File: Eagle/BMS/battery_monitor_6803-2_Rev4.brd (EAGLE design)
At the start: 88.1 x 53.3 mm, 65 parts, among them Q1 MOSFET-PCHANNELIRLML2244, Q10 IRF9530, Q2 MOSFET-NCHANNELBSS138, Q3 MOSFET-PCHANNELIRLML2244, Q4 MOSFET-PCHANNELIRLML2244, Q5 MOSFET-PCHANNELIRLML2244, Q6 MOSFET-NCHANNELBSS138, Q7 MOSFET-NCHANNELBSS138, Q8 MOSFET-NCHANNELBSS138, Q9 PMOS_AO4435

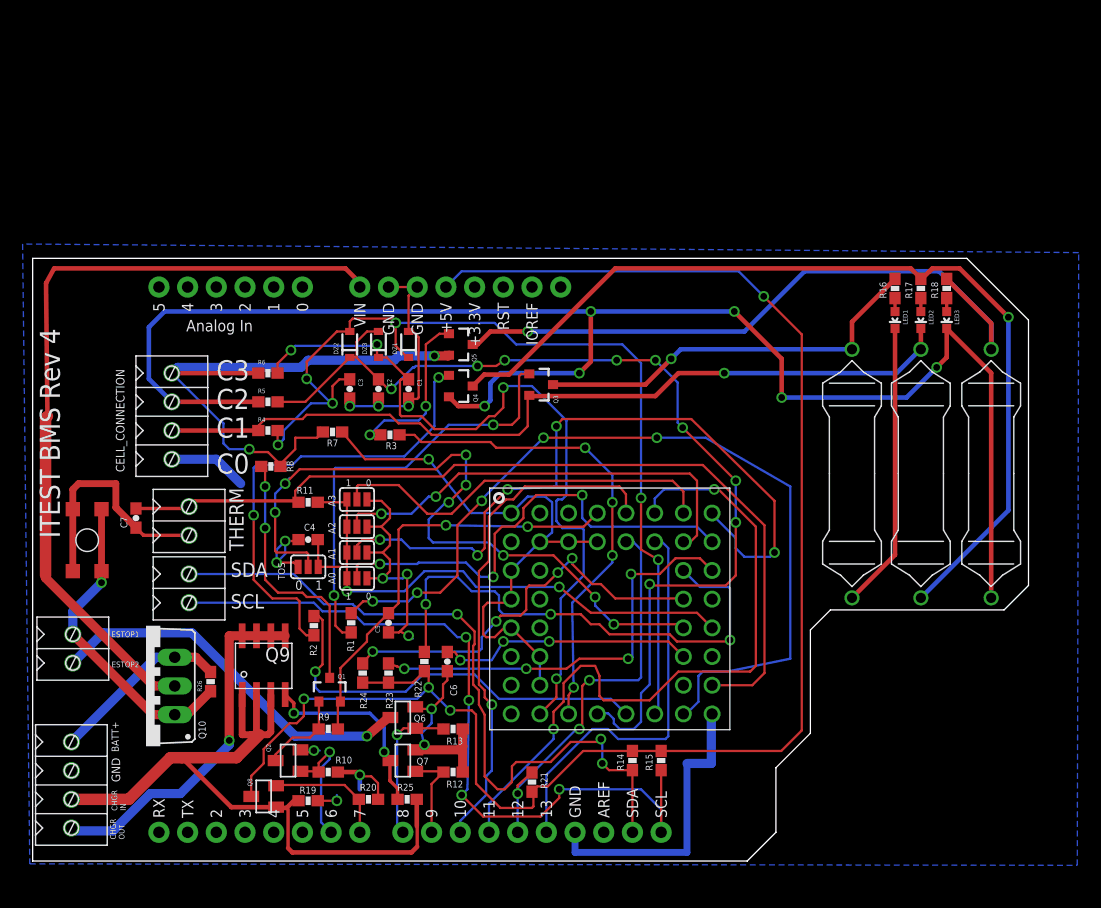
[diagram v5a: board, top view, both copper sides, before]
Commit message: Created encoder board for Layla
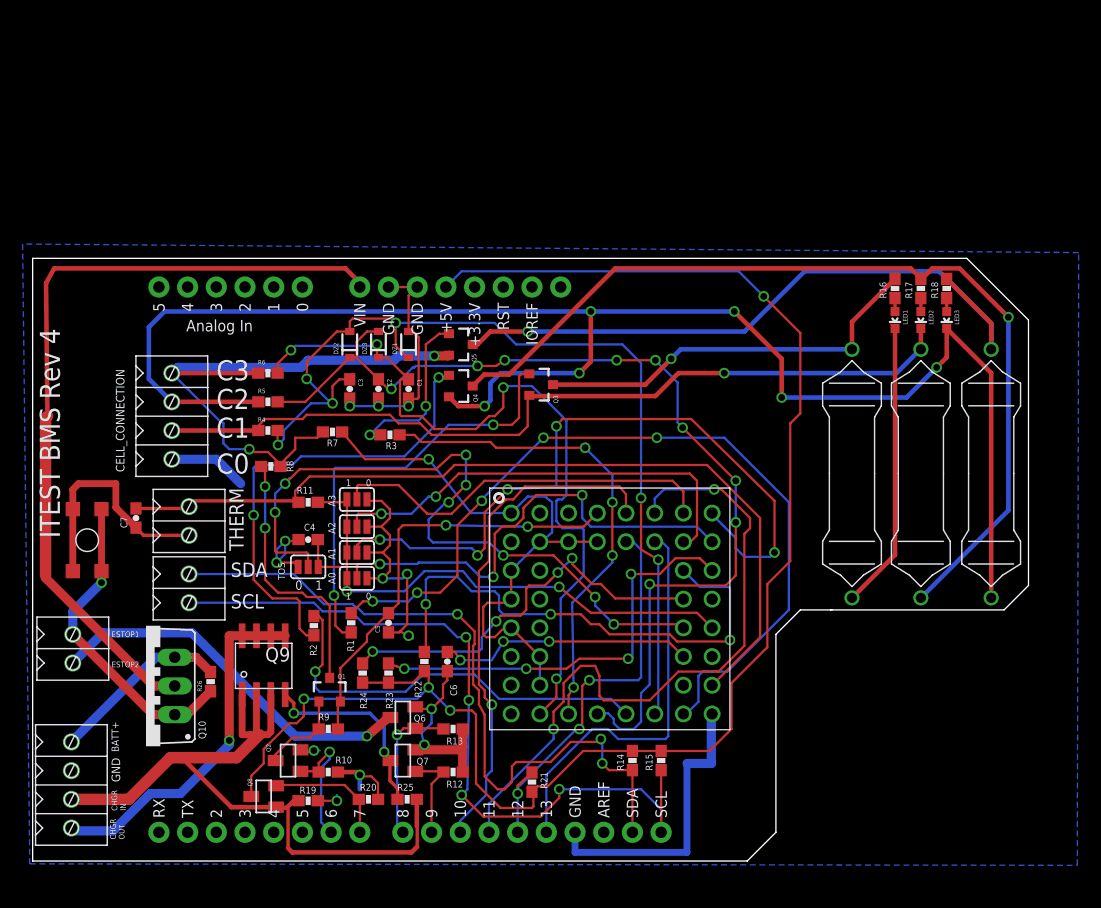
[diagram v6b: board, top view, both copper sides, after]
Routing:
- net +5: track 144.2 -> 140.4 mm
- net S1: track 76.8 -> 74.2 mm
- net VTEMP1: track 78.7 -> 76.5 mm
- net MOSI: track 61.6 -> 60.1 mm
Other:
- outline, holes or cut-outs redrawn
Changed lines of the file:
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@@
 <wire x1="89.662" y1="48.641" x2="89.662" y2="25.146" width="0" layer="20"/>
 <wire x1="67.31" y1="3.302" x2="64.77" y2="0.762" width="0" layer="20"/>
-<wire x1="70.358" y1="21.209" x2="70.358" y2="12.065" width="0" layer="20"/>
-<wire x1="70.358" y1="12.065" x2="67.31" y2="9.017" width="0" layer="20"/>
-<wire x1="67.31" y1="9.017" x2="67.31" y2="3.302" width="0" layer="20"/>
 <wire x1="89.662" y1="48.641" x2="84.201" y2="54.102" width="0" layer="20"/>
 <wire x1="89.662" y1="25.146" x2="87.503" y2="22.987" width="0" layer="20"/>
-<wire x1="72.136" y1="22.987" x2="70.358" y2="21.209" width="0" layer="20"/>
-<wire x1="87.503" y1="22.987" x2="72.136" y2="22.987" width="0" layer="20"/>
+<wire x1="87.503" y1="22.987" x2="72.263" y2="22.987" width="0" layer="20"/>
+<wire x1="72.263" y1="22.987" x2="72.136" y2="22.987" width="0" layer="20"/>
+<wire x1="67.31" y1="3.302" x2="67.31" y2="20.828" width="0" layer="20"/>
+<wire x1="67.31" y1="20.828" x2="69.469" y2="22.987" width="0" layer="20"/>
+<wire x1="69.469" y1="22.987" x2="72.136" y2="22.987" width="0" layer="20"/>
 </plain>
 <attributes>
@@
 <wire x1="31.623" y1="23.749" x2="34.798" y2="23.749" width="0.2032" layer="16"/>
 <wire x1="34.798" y1="23.749" x2="35.56" y2="24.511" width="0.2032" layer="16"/>
-<wire x1="68.58" y1="18.669" x2="68.58" y2="33.909" width="0.2032" layer="16"/>
-<wire x1="68.58" y1="33.909" x2="61.087" y2="38.227" width="0.2032" layer="16"/>
-<wire x1="61.087" y1="38.227" x2="56.769" y2="38.227" width="0.2032" layer="16"/>
+<wire x1="62.738" y1="38.227" x2="56.769" y2="38.227" width="0.2032" layer="16"/>
 <via x="56.769" y="38.227" extent="1-16" drill="0.6"/>
 <wire x1="56.769" y1="38.227" x2="46.736" y2="38.227" width="0.2032" layer="1"/>
@@
 <wire x1="39.116" y1="30.48" x2="39.116" y2="26.035" width="0.2032" layer="1"/>
 <via x="35.56" y="24.511" extent="1-16" drill="0.6"/>
-<wire x1="68.58" y1="18.669" x2="62.992" y2="17.526" width="0.2032" layer="16"/>
 <wire x1="62.992" y1="17.526" x2="60.833" y2="17.526" width="0.2032" layer="16"/>
 <wire x1="60.833" y1="17.526" x2="60.452" y2="17.145" width="0.2032" layer="16"/>
@@
 <wire x1="35.56" y1="24.511" x2="37.592" y2="24.511" width="0.2032" layer="1"/>
 <wire x1="37.592" y1="24.511" x2="39.116" y2="26.035" width="0.2032" layer="1"/>
+<wire x1="62.738" y1="38.227" x2="68.453" y2="32.512" width="0.2032" layer="16"/>
+<wire x1="68.453" y1="32.512" x2="68.453" y2="22.987" width="0.2032" layer="16"/>
+<wire x1="68.453" y1="22.987" x2="62.992" y2="17.526" width="0.2032" layer="16"/>
 </signal>
 <signal name="S2">
@@
 <wire x1="52.07" y1="14.986" x2="56.134" y2="14.986" width="0.2032" layer="1"/>
 <wire x1="56.134" y1="14.986" x2="58.674" y2="17.526" width="0.2032" layer="1"/>
-<wire x1="58.674" y1="17.526" x2="65.024" y2="17.526" width="0.2032" layer="1"/>
-<wire x1="65.024" y1="17.526" x2="65.532" y2="18.034" width="0.2032" layer="1"/>
-<wire x1="65.532" y1="18.034" x2="65.532" y2="30.353" width="0.2032" layer="1"/>
-<wire x1="65.532" y1="30.353" x2="62.23" y2="33.655" width="0.2032" layer="1"/>
 <wire x1="62.23" y1="33.655" x2="61.849" y2="33.655" width="0.2032" layer="1"/>
 <via x="61.849" y="33.655" extent="1-16" drill="0.6"/>
@@
 <wire x1="48.514" y1="14.859" x2="48.514" y2="16.51" width="0.2032" layer="1"/>
 <wire x1="48.514" y1="16.51" x2="50.038" y2="18.034" width="0.2032" layer="1"/>
+<wire x1="58.674" y1="17.526" x2="62.23" y2="17.526" width="0.2032" layer="1"/>
+<wire x1="62.23" y1="17.526" x2="64.516" y2="19.812" width="0.2032" layer="1"/>
+<wire x1="64.516" y1="19.812" x2="64.516" y2="29.718" width="0.2032" layer="1"/>
+<wire x1="64.516" y1="29.718" x2="65.024" y2="30.226" width="0.2032" layer="1"/>
+<wire x1="65.024" y1="30.226" x2="65.024" y2="31.115" width="0.2032" layer="1"/>
+<wire x1="65.024" y1="31.115" x2="62.484" y2="33.655" width="0.2032" layer="1"/>
+<wire x1="62.484" y1="33.655" x2="61.849" y2="33.655" width="0.2032" layer="1"/>
 </signal>
 <signal name="+12">
@@
 <wire x1="26.035" y1="34.798" x2="37.846" y2="34.798" width="0.2032" layer="1"/>
 <wire x1="37.846" y1="34.798" x2="38.862" y2="35.814" width="0.2032" layer="1"/>
-<wire x1="66.294" y1="17.399" x2="65.2145" y2="16.3195" width="0.2032" layer="1"/>
-<wire x1="65.2145" y1="16.3195" x2="61.6585" y2="16.3195" width="0.2032" layer="1"/>
-<wire x1="60.833" y1="35.814" x2="66.294" y2="30.48" width="0.2032" layer="1"/>
-<wire x1="66.294" y1="30.48" x2="66.294" y2="17.399" width="0.2032" layer="1"/>
-<wire x1="38.862" y1="35.814" x2="60.833" y2="35.814" width="0.2032" layer="1"/>
+<wire x1="38.862" y1="35.814" x2="61.214" y2="35.814" width="0.2032" layer="1"/>
+<wire x1="61.214" y1="35.814" x2="65.913" y2="31.115" width="0.2032" layer="1"/>
+<wire x1="65.913" y1="31.115" x2="65.913" y2="20.574" width="0.2032" layer="1"/>
+<wire x1="65.913" y1="20.574" x2="61.6585" y2="16.3195" width="0.2032" layer="1"/>
 </signal>
 <signal name="CHARGE">
@@
 <wire x1="57.15" y1="10.502" x2="57.189" y2="10.541" width="0.2032" layer="1"/>
 <via x="66.2305" y="50.7365" extent="1-16" drill="0.6"/>
-<wire x1="69.596" y1="12.319" x2="69.596" y2="47.371" width="0.2032" layer="1"/>
-<wire x1="69.596" y1="47.371" x2="66.2305" y2="50.7365" width="0.2032" layer="1"/>
 <wire x1="33.02" y1="16.549" x2="35.179" y2="16.549" width="0.2032" layer="1"/>
 <wire x1="35.179" y1="16.549" x2="36.195" y2="17.565" width="0.2032" layer="1"/>
-<wire x1="69.596" y1="12.319" x2="67.779" y2="10.502" width="0.2032" layer="1"/>
-<wire x1="67.779" y1="10.502" x2="57.15" y2="10.502" width="0.2032" layer="1"/>
+<wire x1="68.58" y1="27.305" x2="68.58" y2="39.497" width="0.2032" layer="1"/>
+<wire x1="68.58" y1="39.497" x2="69.469" y2="40.386" width="0.2032" layer="1"/>
+<wire x1="69.469" y1="40.386" x2="69.469" y2="47.498" width="0.2032" layer="1"/>
+<wire x1="69.469" y1="47.498" x2="66.2305" y2="50.7365" width="0.2032" layer="1"/>
+<wire x1="57.15" y1="10.502" x2="61.429" y2="10.502" width="0.2032" layer="1"/>
+<wire x1="61.429" y1="10.502" x2="63.373" y2="12.446" width="0.2032" layer="1"/>
+<wire x1="63.373" y1="12.446" x2="63.373" y2="16.51" width="0.2032" layer="1"/>
+<wire x1="63.373" y1="16.51" x2="66.548" y2="19.685" width="0.2032" layer="1"/>
+<wire x1="66.548" y1="19.685" x2="66.548" y2="25.273" width="0.2032" layer="1"/>
+<wire x1="66.548" y1="25.273" x2="68.58" y2="27.305" width="0.2032" layer="1"/>
 </signal>
 <signal name="SCL">

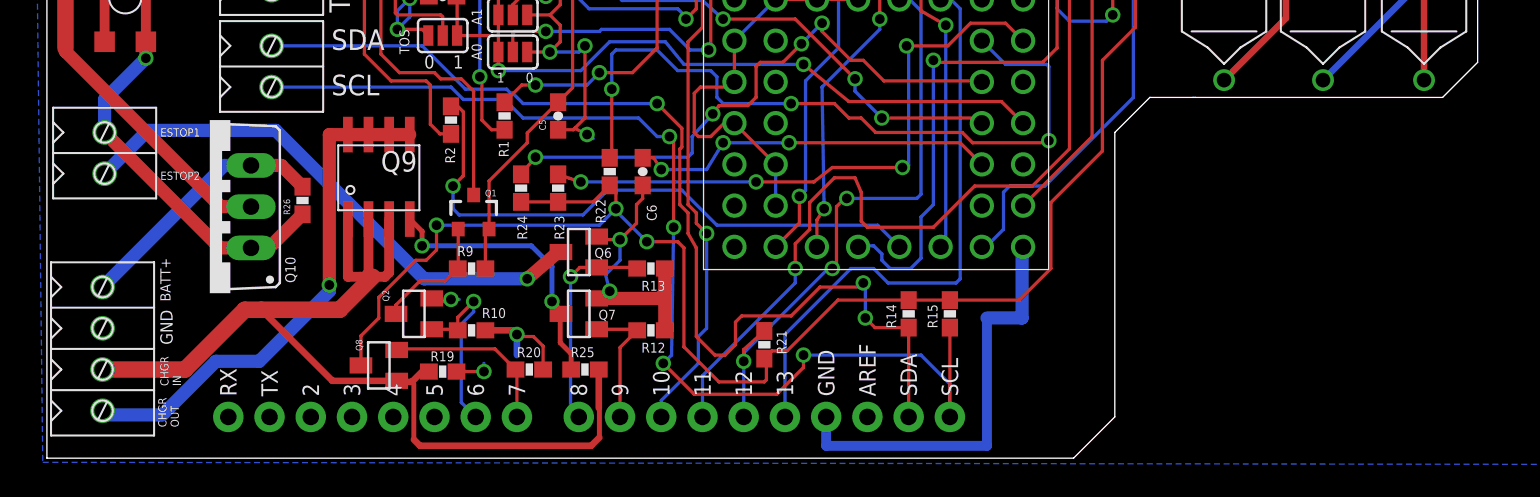
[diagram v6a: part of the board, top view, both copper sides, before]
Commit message: Encoder design Rev1 changes.
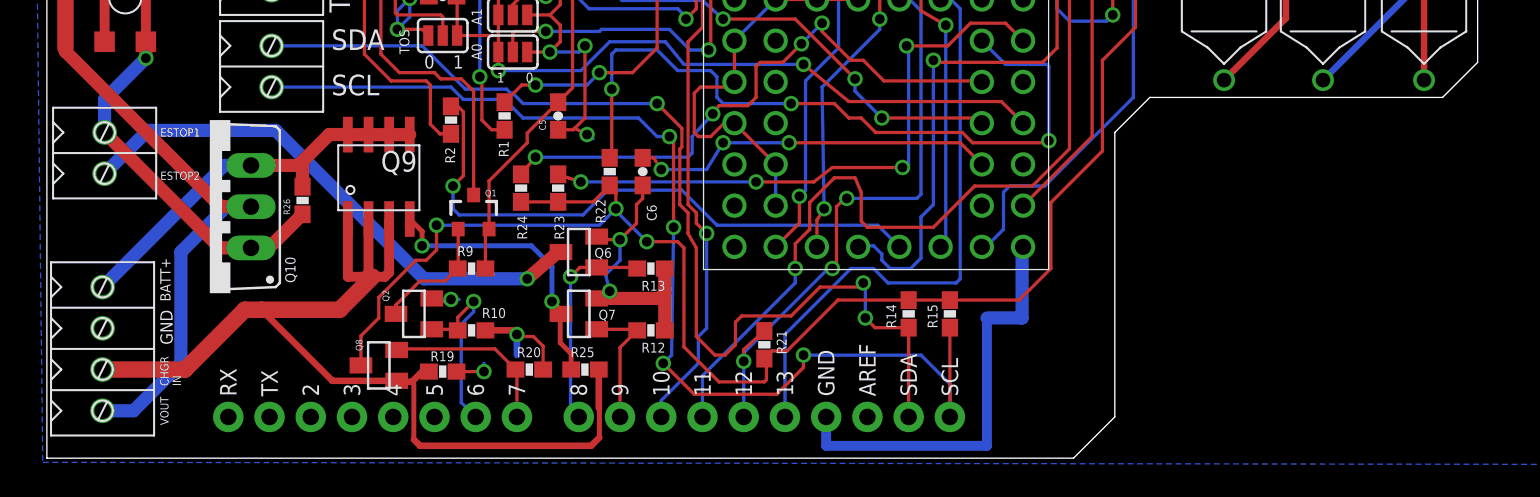
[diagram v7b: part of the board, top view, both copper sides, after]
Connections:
- removed net CHARGER_OUT: Q9.5, Q9.6, Q9.7, Q9.8, U$4.P$4
- net +12: now also U$4.P$4
- net BATTERY+: now also Q9.5, Q9.6, Q9.7, Q9.8
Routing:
- net CHARGER_OUT: track 31.8 -> 0.00 mm, vias 1 -> 0
- net +12: track 71.0 -> 89.4 mm
- net BATTERY+: track 16.0 -> 24.3 mm
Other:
- outline, holes or cut-outs redrawn
- board text added: "VOUT"
- board text removed: "CHGR OUT"
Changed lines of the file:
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@@
 <text x="8.509" y="20.574" size="0.508" layer="21">ESTOP1</text>
 <text x="8.509" y="17.907" size="0.508" layer="21">ESTOP2</text>
-<text x="9.652" y="2.667" size="0.508" layer="21" rot="R90">CHGR
-OUT</text>
+<text x="9.017" y="2.794" size="0.508" layer="21" rot="R90">VOUT</text>
 <wire x1="89.662" y1="48.641" x2="89.662" y2="25.146" width="0" layer="20"/>
 <wire x1="67.31" y1="3.302" x2="64.77" y2="0.762" width="0" layer="20"/>
 <wire x1="89.662" y1="48.641" x2="84.201" y2="54.102" width="0" layer="20"/>
 <wire x1="89.662" y1="25.146" x2="87.503" y2="22.987" width="0" layer="20"/>
-<wire x1="87.503" y1="22.987" x2="72.263" y2="22.987" width="0" layer="20"/>
-<wire x1="72.263" y1="22.987" x2="72.136" y2="22.987" width="0" layer="20"/>
+<wire x1="87.503" y1="22.987" x2="69.469" y2="22.987" width="0" layer="20"/>
 <wire x1="67.31" y1="3.302" x2="67.31" y2="20.828" width="0" layer="20"/>
 <wire x1="67.31" y1="20.828" x2="69.469" y2="22.987" width="0" layer="20"/>
-<wire x1="69.469" y1="22.987" x2="72.136" y2="22.987" width="0" layer="20"/>
 </plain>
 <attributes>
@@
 <wire x1="12.230846875" y1="16.256" x2="2.667" y2="25.819846875" width="0.8128" layer="1"/>
 <wire x1="2.667" y1="25.819846875" x2="2.667" y2="26.035" width="0.8128" layer="1"/>
+<contactref element="U$4" pad="P$4"/>
+<wire x1="4.953" y1="3.683" x2="6.858" y2="3.683" width="0.8128" layer="16"/>
+<wire x1="6.858" y1="3.683" x2="9.779" y2="6.604" width="0.8128" layer="16"/>
+<wire x1="9.779" y1="6.604" x2="9.779" y2="13.462" width="0.8128" layer="16"/>
+<wire x1="9.779" y1="13.462" x2="12.573" y2="16.256" width="0.8128" layer="16"/>
+<wire x1="12.573" y1="16.256" x2="14.097" y2="16.256" width="0.8128" layer="16"/>
 </signal>
 <signal name="VREG">
@@
 <wire x1="24.638" y1="14.732" x2="23.876" y2="15.494" width="0.3048" layer="1"/>
 </signal>
-<signal name="CHARGER_OUT">
-<contactref element="Q9" pad="5"/>
-<contactref element="Q9" pad="6"/>
-<contactref element="Q9" pad="7"/>
-<contactref element="Q9" pad="8"/>
-<wire x1="20.066" y1="20.694" x2="21.336" y2="20.694" width="0.8128" layer="1"/>
-<wire x1="21.336" y1="20.694" x2="22.606" y2="20.694" width="0.8128" layer="1"/>
-<wire x1="22.606" y1="20.694" x2="23.876" y2="20.694" width="0.8128" layer="1"/>
-<contactref element="U$4" pad="P$4"/>
-<wire x1="20.066" y1="20.694" x2="18.923" y2="20.694" width="0.8128" layer="1"/>
-<wire x1="18.923" y1="20.694" x2="18.923" y2="11.43" width="0.8128" layer="1"/>
-<via x="18.923" y="11.43" extent="1-16" drill="0.6"/>
-<wire x1="18.923" y1="11.43" x2="18.923" y2="11.049" width="0.8128" layer="16"/>
-<wire x1="18.923" y1="11.049" x2="14.605" y2="6.731" width="0.8128" layer="16"/>
-<wire x1="14.605" y1="6.731" x2="11.938" y2="6.731" width="0.8128" layer="16"/>
-<wire x1="11.938" y1="6.731" x2="8.636" y2="3.429" width="0.8128" layer="16"/>
-<wire x1="8.636" y1="3.429" x2="5.207" y2="3.429" width="0.8128" layer="16"/>
-<wire x1="5.207" y1="3.429" x2="4.953" y2="3.683" width="0.8128" layer="16"/>
-</signal>
 <signal name="ESTOP2">
 <wire x1="33.02" y1="13.462" x2="31.115" y2="11.811" width="0.8128" layer="1"/>
@@
 <signal name="BATTERY+">
 <contactref element="Q10" pad="S"/>
-<wire x1="14.097" y1="18.796" x2="15.963" y2="18.796" width="0.8128" layer="1"/>
+<wire x1="14.097" y1="18.796" x2="17.272" y2="18.796" width="0.8128" layer="1"/>
 <contactref element="U$4" pad="P$1"/>
 <contactref element="R26" pad="2"/>
-<wire x1="17.272" y1="17.487" x2="15.963" y2="18.796" width="0.8128" layer="1"/>
 <wire x1="4.953" y1="11.303" x2="12.446" y2="18.796" width="0.8128" layer="16"/>
 <wire x1="12.446" y1="18.796" x2="14.097" y2="18.796" width="0.8128" layer="16"/>
+<contactref element="Q9" pad="8"/>
+<contactref element="Q9" pad="7"/>
+<contactref element="Q9" pad="5"/>
+<contactref element="Q9" pad="6"/>
+<wire x1="23.876" y1="20.694" x2="22.606" y2="20.694" width="0.8128" layer="1"/>
+<wire x1="22.606" y1="20.694" x2="21.336" y2="20.694" width="0.8128" layer="1"/>
+<wire x1="21.336" y1="20.694" x2="20.066" y2="20.694" width="0.8128" layer="1"/>
+<wire x1="20.066" y1="20.694" x2="20.059" y2="20.701" width="0.8128" layer="1"/>
+<wire x1="20.059" y1="20.701" x2="18.923" y2="20.701" width="0.8128" layer="1"/>
+<wire x1="18.923" y1="20.701" x2="17.272" y2="19.05" width="0.8128" layer="1"/>
+<wire x1="17.272" y1="19.05" x2="17.272" y2="18.796" width="0.8128" layer="1"/>
+<wire x1="17.272" y1="18.796" x2="17.272" y2="17.487" width="0.8128" layer="1"/>
 </signal>
 <signal name="ESTOP1">
